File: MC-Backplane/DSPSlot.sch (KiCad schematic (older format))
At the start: 1 part

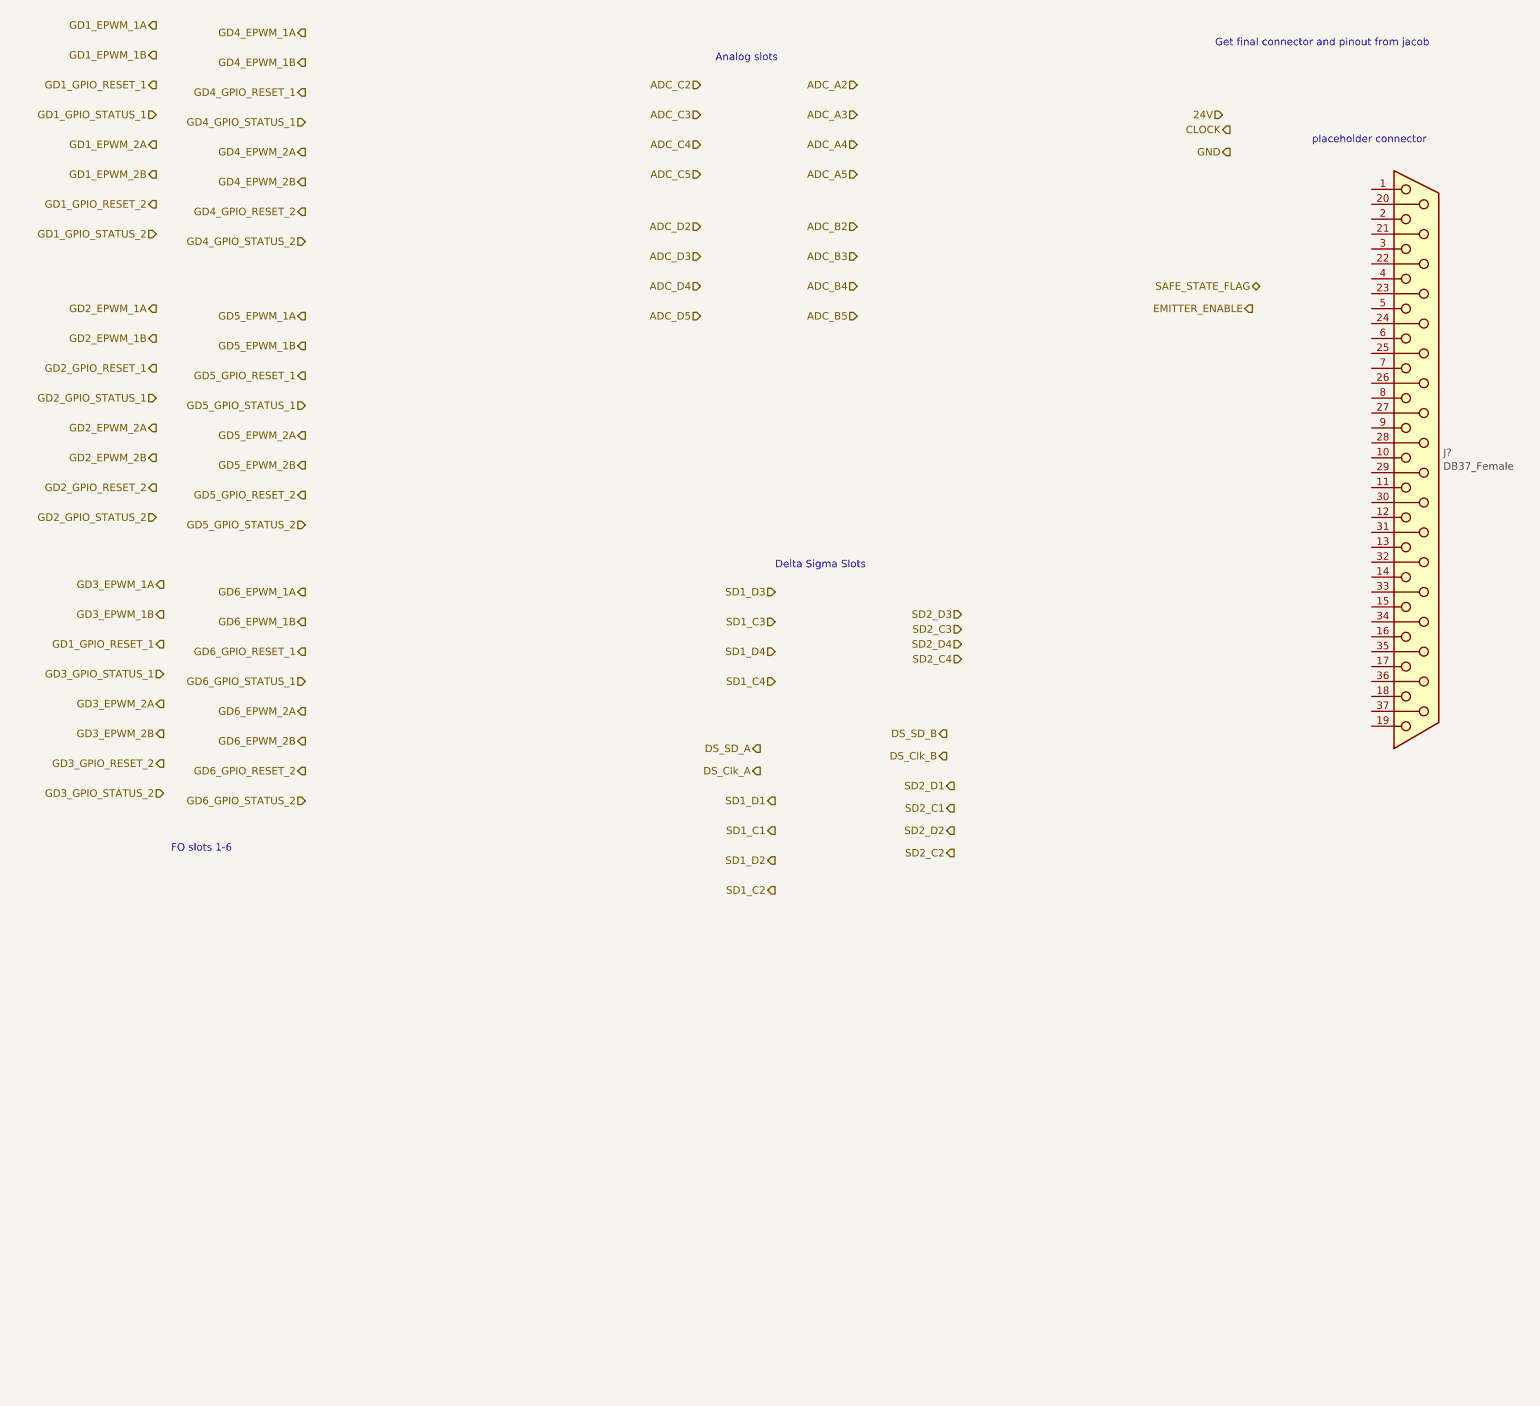
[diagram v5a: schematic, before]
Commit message: Prep for DSP connector
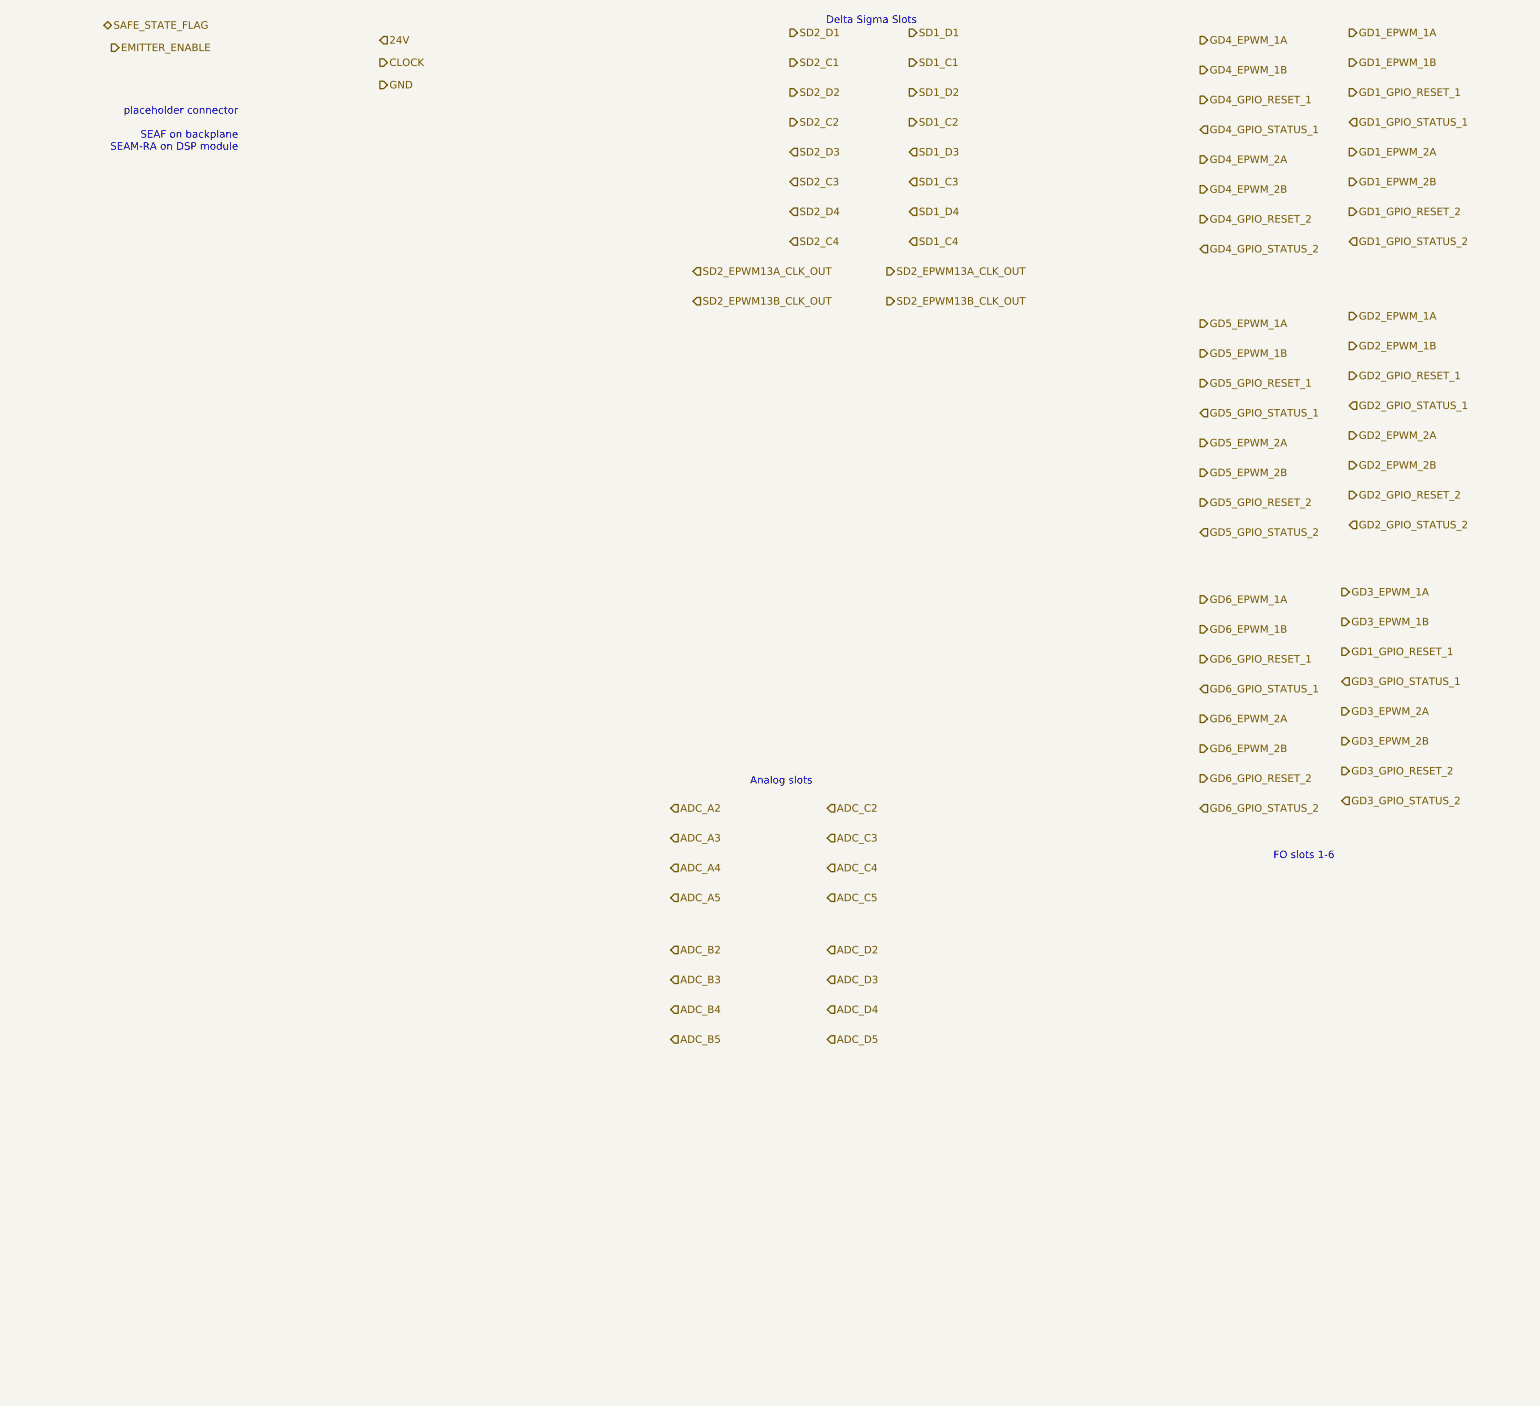
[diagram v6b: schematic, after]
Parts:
- removed J?: DB37_Female, symbol Connector:DB37_Female
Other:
- note added: "placeholder connector\n\nSEAF on backplane\nSEAM-RA on DSP module"
- note removed: "Get final connector and pinout from jacob"
- note removed: "placeholder connector"
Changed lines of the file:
@@
 $Descr A4 11693 8268
 encoding utf-8
-Sheet 3 7
+Sheet 6 7
 Title ""
 Date ""
@@
 Comment4 ""
 $EndDescr
-$Comp
-L Connector:DB37_Female J?
-U 1 1 61EE6699
-P 10100 3650
-F 0 "J?" H 10280 3684 50  0000 L CNN
-F 1 "DB37_Female" H 10280 3593 50  0000 L CNN
-F 2 "" H 10100 3650 50  0001 C CNN
-F 3 " ~" H 10100 3650 50  0001 C CNN
-	1    10100 3650
-	1    0    0    -1
-$EndComp
-Text Notes 9400 1550 0    50   ~ 0
-placeholder connector
-Text HLabel 1650 750  0    50   Output ~ 0
+Text Notes 2200 1600 2    50   ~ 0
+placeholder connector\n\nSEAF on backplane\nSEAM-RA on DSP module
+Text HLabel 9650 800  2    50   Output ~ 0
 GD1_EPWM_1A
-Text HLabel 1650 950  0    50   Output ~ 0
+Text HLabel 9650 1000 2    50   Output ~ 0
 GD1_EPWM_1B
-Text HLabel 1650 1150 0    50   Output ~ 0
+Text HLabel 9650 1200 2    50   Output ~ 0
 GD1_GPIO_RESET_1
-Text HLabel 1650 1350 0    50   Input ~ 0
+Text HLabel 9650 1400 2    50   Input ~ 0
 GD1_GPIO_STATUS_1
-Text HLabel 1650 1550 0    50   Output ~ 0
+Text HLabel 9650 1600 2    50   Output ~ 0
 GD1_EPWM_2A
-Text HLabel 1650 1750 0    50   Output ~ 0
+Text HLabel 9650 1800 2    50   Output ~ 0
 GD1_EPWM_2B
-Text HLabel 1650 1950 0    50   Output ~ 0
+Text HLabel 9650 2000 2    50   Output ~ 0
 GD1_GPIO_RESET_2
-Text HLabel 1650 2150 0    50   Input ~ 0
+Text HLabel 9650 2200 2    50   Input ~ 0
 GD1_GPIO_STATUS_2
-Text HLabel 1650 2650 0    50   Output ~ 0
+Text HLabel 9650 2700 2    50   Output ~ 0
 GD2_EPWM_1A
-Text HLabel 1650 2850 0    50   Output ~ 0
+Text HLabel 9650 2900 2    50   Output ~ 0
 GD2_EPWM_1B
-Text HLabel 1650 3050 0    50   Output ~ 0
+Text HLabel 9650 3100 2    50   Output ~ 0
 GD2_GPIO_RESET_1
-Text HLabel 1650 3250 0    50   Input ~ 0
+Text HLabel 9650 3300 2    50   Input ~ 0
 GD2_GPIO_STATUS_1
-Text HLabel 1650 3450 0    50   Output ~ 0
+Text HLabel 9650 3500 2    50   Output ~ 0
 GD2_EPWM_2A
-Text HLabel 1650 3650 0    50   Output ~ 0
+Text HLabel 9650 3700 2    50   Output ~ 0
 GD2_EPWM_2B
-Text HLabel 1650 3850 0    50   Output ~ 0
+Text HLabel 9650 3900 2    50   Output ~ 0
 GD2_GPIO_RESET_2
-Text HLabel 1650 4050 0    50   Input ~ 0
+Text HLabel 9650 4100 2    50   Input ~ 0
 GD2_GPIO_STATUS_2
-Text HLabel 1700 4500 0    50   Output ~ 0
+Text HLabel 9600 4550 2    50   Output ~ 0
 GD3_EPWM_1A
-Text HLabel 1700 4700 0    50   Output ~ 0
+Text HLabel 9600 4750 2    50   Output ~ 0
 GD3_EPWM_1B
-Text HLabel 1700 4900 0    50   Output ~ 0
+Text HLabel 9600 4950 2    50   Output ~ 0
 GD1_GPIO_RESET_1
-Text HLabel 1700 5100 0    50   Input ~ 0
+Text HLabel 9600 5150 2    50   Input ~ 0
 GD3_GPIO_STATUS_1
-Text HLabel 1700 5300 0    50   Output ~ 0
+Text HLabel 9600 5350 2    50   Output ~ 0
 GD3_EPWM_2A
-Text HLabel 1700 5500 0    50   Output ~ 0
+Text HLabel 9600 5550 2    50   Output ~ 0
 GD3_EPWM_2B
-Text HLabel 1700 5700 0    50   Output ~ 0
+Text HLabel 9600 5750 2    50   Output ~ 0
 GD3_GPIO_RESET_2
-Text HLabel 1700 5900 0    50   Input ~ 0
+Text HLabel 9600 5950 2    50   Input ~ 0
 GD3_GPIO_STATUS_2
-Text HLabel 2650 800  0    50   Output ~ 0
+Text HLabel 8650 850  2    50   Output ~ 0
 GD4_EPWM_1A
-Text HLabel 2650 1000 0    50   Output ~ 0
+Text HLabel 8650 1050 2    50   Output ~ 0
 GD4_EPWM_1B
-Text HLabel 2650 1200 0    50   Output ~ 0
+Text HLabel 8650 1250 2    50   Output ~ 0
 GD4_GPIO_RESET_1
-Text HLabel 2650 1400 0    50   Input ~ 0
+Text HLabel 8650 1450 2    50   Input ~ 0
 GD4_GPIO_STATUS_1
-Text HLabel 2650 1600 0    50   Output ~ 0
+Text HLabel 8650 1650 2    50   Output ~ 0
 GD4_EPWM_2A
-Text HLabel 2650 1800 0    50   Output ~ 0
+Text HLabel 8650 1850 2    50   Output ~ 0
 GD4_EPWM_2B
-Text HLabel 2650 2000 0    50   Output ~ 0
+Text HLabel 8650 2050 2    50   Output ~ 0
 GD4_GPIO_RESET_2
-Text HLabel 2650 2200 0    50   Input ~ 0
+Text HLabel 8650 2250 2    50   Input ~ 0
 GD4_GPIO_STATUS_2
-Text HLabel 2650 4100 0    50   Input ~ 0
+Text HLabel 8650 4150 2    50   Input ~ 0
 GD5_GPIO_STATUS_2
-Text HLabel 2650 3900 0    50   Output ~ 0
+Text HLabel 8650 3950 2    50   Output ~ 0
 GD5_GPIO_RESET_2
-Text HLabel 2650 3700 0    50   Output ~ 0
+Text HLabel 8650 3750 2    50   Output ~ 0
 GD5_EPWM_2B
-Text HLabel 2650 3500 0    50   Output ~ 0
+Text HLabel 8650 3550 2    50   Output ~ 0
 GD5_EPWM_2A
-Text HLabel 2650 3300 0    50   Input ~ 0
+Text HLabel 8650 3350 2    50   Input ~ 0
 GD5_GPIO_STATUS_1
-Text HLabel 2650 3100 0    50   Output ~ 0
+Text HLabel 8650 3150 2    50   Output ~ 0
 GD5_GPIO_RESET_1
-Text HLabel 2650 2900 0    50   Output ~ 0
+Text HLabel 8650 2950 2    50   Output ~ 0
 GD5_EPWM_1B
-Text HLabel 2650 2700 0    50   Output ~ 0
+Text HLabel 8650 2750 2    50   Output ~ 0
 GD5_EPWM_1A
-Text HLabel 2650 5950 0    50   Input ~ 0
+Text HLabel 8650 6000 2    50   Input ~ 0
 GD6_GPIO_STATUS_2
-Text HLabel 2650 5750 0    50   Output ~ 0
+Text HLabel 8650 5800 2    50   Output ~ 0
 GD6_GPIO_RESET_2
-Text HLabel 2650 5550 0    50   Output ~ 0
+Text HLabel 8650 5600 2    50   Output ~ 0
 GD6_EPWM_2B
-Text HLabel 2650 5350 0    50   Output ~ 0
+Text HLabel 8650 5400 2    50   Output ~ 0
 GD6_EPWM_2A
-Text HLabel 2650 5150 0    50   Input ~ 0
+Text HLabel 8650 5200 2    50   Input ~ 0
 GD6_GPIO_STATUS_1
-Text HLabel 2650 4950 0    50   Output ~ 0
+Text HLabel 8650 5000 2    50   Output ~ 0
 GD6_GPIO_RESET_1
-Text HLabel 2650 4750 0    50   Output ~ 0
+Text HLabel 8650 4800 2    50   Output ~ 0
 GD6_EPWM_1B
-Text HLabel 2650 4550 0    50   Output ~ 0
+Text HLabel 8650 4600 2    50   Output ~ 0
 GD6_EPWM_1A
-Text Notes 1750 6300 0    50   ~ 0
+Text Notes 9550 6350 2    50   ~ 0
 FO slots 1-6
-Text HLabel 8850 1450 0    50   Output ~ 0
+Text HLabel 3150 1000 2    50   Output ~ 0
 CLOCK
-Text HLabel 9000 2650 0    50   Output ~ 0
+Text HLabel 1350 900  2    50   Output ~ 0
 EMITTER_ENABLE
-Text HLabel 9050 2500 0    50   BiDi ~ 0
+Text HLabel 1300 750  2    50   BiDi ~ 0
 SAFE_STATE_FLAG
-Text HLabel 8850 1600 0    50   Output ~ 0
+Text HLabel 3150 1150 2    50   Output ~ 0
 GND
-Text HLabel 8800 1350 0    50   Input ~ 0
+Text HLabel 3150 850  2    50   Input ~ 0
 24V
-Text HLabel 5800 5950 0    50   Output ~ 0
+Text HLabel 6700 800  2    50   Output ~ 0
 SD1_D1
-Text HLabel 5800 6150 0    50   Output ~ 0
+Text HLabel 6700 1000 2    50   Output ~ 0
 SD1_C1
-Text HLabel 5800 6350 0    50   Output ~ 0
+Text HLabel 6700 1200 2    50   Output ~ 0
 SD1_D2
-Text HLabel 5800 6550 0    50   Output ~ 0
+Text HLabel 6700 1400 2    50   Output ~ 0
 SD1_C2
-Text HLabel 5700 5600 0    50   Output ~ 0
-DS_SD_A
-Text HLabel 5700 5750 0    50   Output ~ 0
-DS_Clk_A
-Text HLabel 5800 4550 0    50   Input ~ 0
+Text HLabel 6700 1600 2    50   Input ~ 0
 SD1_D3
-Text HLabel 5800 4750 0    50   Input ~ 0
+Text HLabel 6700 1800 2    50   Input ~ 0
 SD1_C3
-Text HLabel 5800 4950 0    50   Input ~ 0
+Text HLabel 6700 2000 2    50   Input ~ 0
 SD1_D4
-Text HLabel 5800 5150 0    50   Input ~ 0
+Text HLabel 6700 2200 2    50   Input ~ 0
 SD1_C4
-Text HLabel 7000 5850 0    50   Output ~ 0
+Text HLabel 5900 800  2    50   Output ~ 0
 SD2_D1
-Text HLabel 7000 6000 0    50   Output ~ 0
+Text HLabel 5900 1000 2    50   Output ~ 0
 SD2_C1
-Text HLabel 7000 6150 0    50   Output ~ 0
+Text HLabel 5900 1200 2    50   Output ~ 0
 SD2_D2
-Text HLabel 7000 6300 0    50   Output ~ 0
+Text HLabel 5900 1400 2    50   Output ~ 0
 SD2_C2
-Text HLabel 6950 5500 0    50   Output ~ 0
-DS_SD_B
-Text HLabel 6950 5650 0    50   Output ~ 0
-DS_Clk_B
-Text HLabel 7050 4700 0    50   Input ~ 0
+Text HLabel 5900 1600 2    50   Input ~ 0
 SD2_D3
-Text HLabel 7050 4800 0    50   Input ~ 0
+Text HLabel 5900 1800 2    50   Input ~ 0
 SD2_C3
-Text HLabel 7050 4900 0    50   Input ~ 0
+Text HLabel 5900 2000 2    50   Input ~ 0
 SD2_D4
-Text HLabel 7050 5000 0    50   Input ~ 0
+Text HLabel 5900 2200 2    50   Input ~ 0
 SD2_C4
-Text Notes 5400 1000 0    50   ~ 0
+Text Notes 6050 5850 2    50   ~ 0
 Analog slots
-Text Notes 5800 4400 0    50   ~ 0
+Text Notes 6750 750  2    50   ~ 0
 Delta Sigma Slots
-Text Notes 8750 900  0    50   ~ 0
-Get final connector and pinout from jacob
-Text HLabel 6350 1150 0    50   Input ~ 0
+Text HLabel 5100 6000 2    50   Input ~ 0
 ADC_A2
-Text HLabel 6350 1350 0    50   Input ~ 0
+Text HLabel 5100 6200 2    50   Input ~ 0
 ADC_A3
-Text HLabel 6350 1550 0    50   Input ~ 0
+Text HLabel 5100 6400 2    50   Input ~ 0
 ADC_A4
-Text HLabel 6350 1750 0    50   Input ~ 0
+Text HLabel 5100 6600 2    50   Input ~ 0
 ADC_A5
-Text HLabel 6350 2100 0    50   Input ~ 0
+Text HLabel 5100 6950 2    50   Input ~ 0
 ADC_B2
-Text HLabel 6350 2300 0    50   Input ~ 0
+Text HLabel 5100 7150 2    50   Input ~ 0
 ADC_B3
-Text HLabel 5300 1150 0    50   Input ~ 0
+Text HLabel 6150 6000 2    50   Input ~ 0
 ADC_C2
-Text HLabel 5300 1350 0    50   Input ~ 0
+Text HLabel 6150 6200 2    50   Input ~ 0
 ADC_C3
-Text HLabel 5300 1550 0    50   Input ~ 0
+Text HLabel 6150 6400 2    50   Input ~ 0
 ADC_C4
-Text HLabel 5300 1750 0    50   Input ~ 0
+Text HLabel 6150 6600 2    50   Input ~ 0
 ADC_C5
-Text HLabel 6350 2500 0    50   Input ~ 0
+Text HLabel 5100 7350 2    50   Input ~ 0
 ADC_B4
-Text HLabel 6350 2700 0    50   Input ~ 0
+Text HLabel 5100 7550 2    50   Input ~ 0
 ADC_B5
-Text HLabel 5300 2100 0    50   Input ~ 0
+Text HLabel 6150 6950 2    50   Input ~ 0
 ADC_D2
-Text HLabel 5300 2300 0    50   Input ~ 0
+Text HLabel 6150 7150 2    50   Input ~ 0
 ADC_D3
-Text HLabel 5300 2500 0    50   Input ~ 0
+Text HLabel 6150 7350 2    50   Input ~ 0
 ADC_D4
-Text HLabel 5300 2700 0    50   Input ~ 0
+Text HLabel 6150 7550 2    50   Input ~ 0
 ADC_D5
+Text HLabel 6550 2400 2    50   Output ~ 0
+SD2_EPWM13A_CLK_OUT
+Text HLabel 6550 2600 2    50   Output ~ 0
+SD2_EPWM13B_CLK_OUT
+Text HLabel 5250 2400 2    50   Input ~ 0
+SD2_EPWM13A_CLK_OUT
+Text HLabel 5250 2600 2    50   Input ~ 0
+SD2_EPWM13B_CLK_OUT
 $EndSCHEMATC

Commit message: DSP interface pin out
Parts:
- added J?: 374472, 374472, symbol Existing_IC_Models:374472
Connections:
- net 24V: now also J?.B8, J?.D8
- net ADC_A2: now also J?.A3
- net ADC_A3: now also J?.D2
- net ADC_A4: now also J?.C5
- net ADC_A5: now also J?.A5
- net ADC_B2: now also J?.B2
- net ADC_B3: now also J?.E1
- net ADC_B4: now also J?.A7
- net ADC_B5: now also J?.D6
- net ADC_C2: now also J?.C1
- net ADC_C3: now also J?.A1
- net ADC_C4: now also J?.D4
- net ADC_C5: now also J?.B4
- net ADC_D2: now also J?.B6
- net ADC_D3: now also J?.E5
- net CLOCK: now also J?.A17
- net GD6_EPWM_1A: now also J?.A19
- net GD6_EPWM_1B: now also J?.D18
- net GD6_EPWM_2A: now also J?.E19
- net GD6_EPWM_2B: now also J?.C19
- net GND: now also J?.A10, J?.A12, J?.A14, J?.A16, J?.A18, J?.A2, J?.A20, J?.A22, J?.A24, J?.A26, J?.A28, J?.A30, J?.A32, J?.A4, J?.A6, J?.A8, J?.B1, J?.B11, J?.B13, J?.B15, J?.B17, J?.B19, J?.B21, J?.B23, J?.B25, J?.B27, J?.B29, J?.B3, J?.B31, J?.B5, J?.B7, J?.B9, J?.C10, J?.C12, J?.C14, J?.C16, J?.C18, J?.C2, J?.C20, J?.C22, J?.C24, J?.C26, J?.C28, J?.C30, J?.C32, J?.C4, J?.C6, J?.C8, J?.D1, J?.D11, J?.D13, J?.D15, J?.D17, J?.D19, J?.D21, J?.D23, J?.D25, J?.D27, J?.D29, J?.D3, J?.D31, J?.D5, J?.D7, J?.D9, J?.E10, J?.E12, J?.E14, J?.E16, J?.E18, J?.E2, J?.E20, J?.E22, J?.E24, J?.E26, J?.E28, J?.E30, J?.E32, J?.E4, J?.E6, J?.E8
- net SD1_C1: now also J?.C13
- net SD1_C2: now also J?.B14
- net SD1_C3: now also J?.A15
- net SD1_C4: now also J?.E15
- net SD1_D1: now also J?.A13
- net SD1_D2: now also J?.E13
- net SD1_D3: now also J?.D14
- net SD1_D4: now also J?.C15
- net SD2_C1: now also J?.B10
- net SD2_C2: now also J?.A11
- net SD2_C3: now also J?.E11
- net SD2_C4: now also J?.C9
- net SD2_D1: now also J?.E9
- net SD2_D2: now also J?.D10
- net SD2_D3: now also J?.C11
- net SD2_D4: now also J?.A9
- net SD2_EPWM13A_CLK_OUT: now also J?.D16
- net SD2_EPWM13B_CLK_OUT: now also J?.B16
- new net ADC_14: J?.E7
- new net ADC_15: J?.C7
- new net ADC_D0: J?.E3
- new net ADC_D1: J?.C3
- new net GD1_EPWM_11A: J?.A31
- new net GD1_EPWM_11B: J?.D30
- new net GD1_EPWM_12A: J?.E31
- new net GD1_EPWM_12B: J?.C31
- new net GD1_GPIO52_STATUS_2: J?.B32
- new net GD1_GPIO53_STATUS_1: J?.D32
- new net GD2_EPWM_10A: J?.C29
- new net GD2_EPWM_10B: J?.A29
- new net GD2_EPWM_9A: J?.D28
- new net GD2_EPWM_9B: J?.B28
- new net GD2_GPIO44_STATUS_2: J?.E29
- new net GD2_GPIO45_STATUS_1: J?.B30
- new net GD3_EPWM_7A: J?.B26
- new net GD3_EPWM_7B: J?.E25
- new net GD3_EPWM_8A: J?.A27
- new net GD3_EPWM_8B: J?.D26
- new net GD3_GPIO24_STATUS_2: J?.C27
- new net GD3_GPIO25_STATUS_1: J?.E27
- new net GD4_GPIO22_STATUS_2: J?.A25
- new net GD4_GPIO23_STATUS_1: J?.C25
- new net GD5_EPWM_3A: J?.C21
- new net GD5_EPWM_3B: J?.A21
- new net GD5_EPWM_4A: J?.B22
- new net GD5_EPWM_4B: J?.E21
- new net GD5_GPIO18_STATUS_2: J?.D22
- new net GD5_GPIO19_STATUS_1: J?.A23
- new net GD6_GPIO15_STATUS_2: J?.B20
- new net GD6_GPIO16_STATUS_1: J?.D20
- new net GD_EPWM_5A: J?.E23
- new net GD_EPWM_5B: J?.C23
- new net GD_EPWM_6A: J?.D24
- new net GD_EPWM_6B: J?.B24
- new net GD_GPIO14_RESET: J?.B18
- new net GPIO12_EMITTER_ENABLE: J?.C17
- new net SD1_EPWM14A_CLK_OUT: J?.D12
- new net SD1_EPWM14B_CLK_OUT: J?.B12
- new net ~GPIO13_SAFE_STATE_FLAG~: J?.E17
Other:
- note added: "1"
- note added: "32"
- note added: "DSP"
- note added: "Gate driver"
- note added: "a"
- note added: "adc"
- note added: "delta sigma"
- note added: "e"
- note removed: "Analog slots"
- note removed: "Delta Sigma Slots"
- note removed: "FO slots 1-6"
- note removed: "placeholder connector\n\nSEAF on backplane\nSEAM-RA on DSP module"
